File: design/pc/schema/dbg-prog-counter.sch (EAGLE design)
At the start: 7 parts, among them IC1 74160N, IC2 74160N, IC3 74160N, IC4 74160N, IC5 74LS245N, IC6 74LS245N, IC7 74LS04N

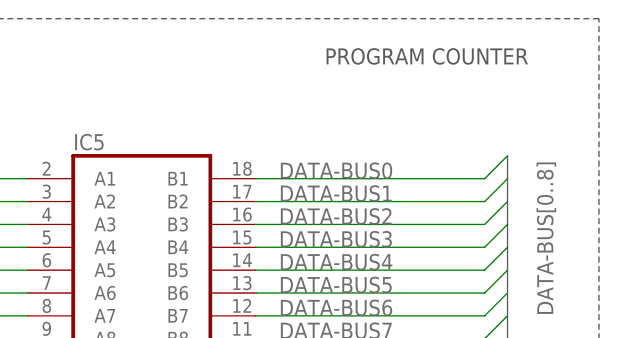
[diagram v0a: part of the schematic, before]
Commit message: Aligned titles size for all schemas
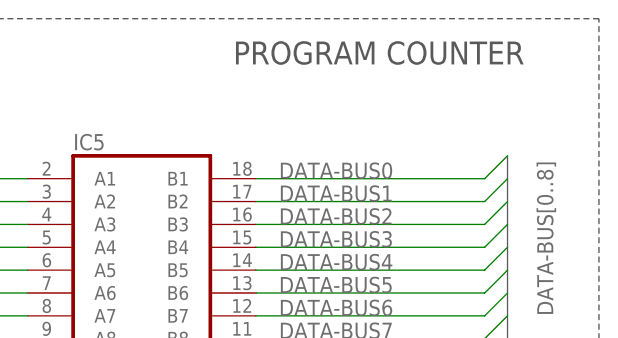
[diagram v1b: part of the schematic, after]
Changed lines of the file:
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@@
 <wire x1="0" y1="-2.54" x2="0" y2="160.02" width="0.1524" layer="97" style="shortdash"/>
 <wire x1="0" y1="160.02" x2="-185.42" y2="160.02" width="0.1524" layer="97" style="shortdash"/>
-<text x="-30.48" y="154.94" size="1.778" layer="97">PROGRAM COUNTER</text>
+<text x="-40.64" y="154.94" size="2.54" layer="97">PROGRAM COUNTER</text>
 </plain>
 <instances>
